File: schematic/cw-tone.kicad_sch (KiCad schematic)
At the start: 21 parts, among them Q14 2N7000, Q15 2N7000, U16 NE5532

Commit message: Minor changes
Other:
- moved on the sheet: C134, C135, C136, C137, C138, C139, C140, C141, D19, D20, Q14, Q15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

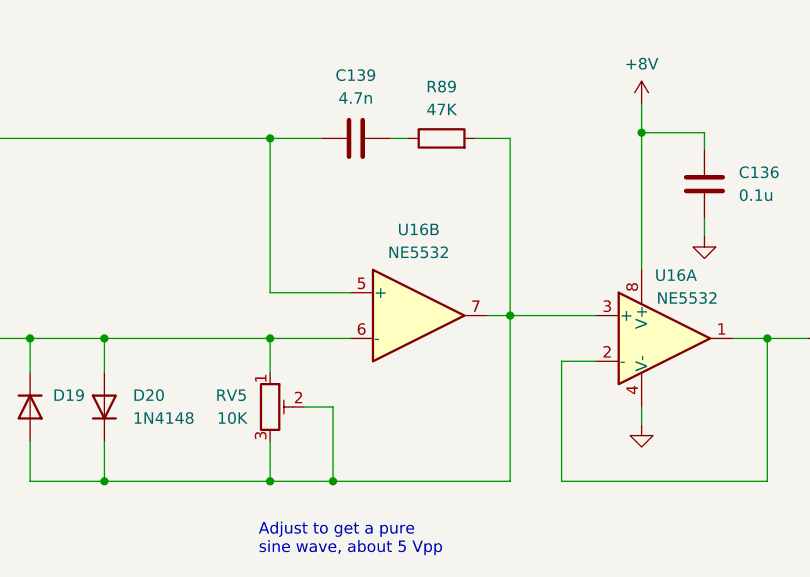
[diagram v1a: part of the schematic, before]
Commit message: Make CW tone frequency adjustable
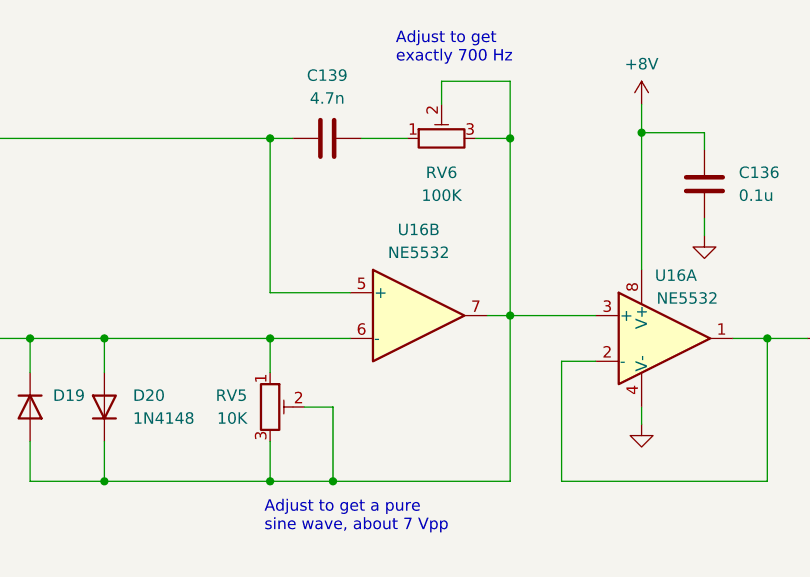
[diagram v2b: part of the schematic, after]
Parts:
- removed R89: 47K, symbol Device:R
- added RV6: 100K, symbol Device:R_Potentiometer_Trim
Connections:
- net at D19.2 (A), D20.1 (K), RV5.2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: now also RV6.2, RV6.3
- net at C139.2: now also RV6.1
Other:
- note added: "Adjust to get a pure sine wave, about 7 Vpp"
- note added: "Adjust to get exactly 700 Hz"
- note removed: "Adjust to get a pure sine wave, about 5 Vpp"
- moved on the sheet: C139
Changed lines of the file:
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@@
   (junction (at 77.47 99.695) (diameter 0) (color 0 0 0 0)
   )
+  (junction (at 130.81 77.47) (diameter 0) (color 0 0 0 0)
+  )
   (junction (at 130.81 97.155) (diameter 0) (color 0 0 0 0)
   )
+  (junction (at 85.725 99.695) (diameter 0) (color 0 0 0 0)
+  )
   (junction (at 104.14 77.47) (diameter 0) (color 0 0 0 0)
   )
-  (junction (at 85.725 99.695) (diameter 0) (color 0 0 0 0)
-  )
   (junction (at 210.185 71.12) (diameter 0) (color 0 0 0 0)
   )
@@
     (stroke (width 0) (type default))
   )
+  (wire (pts (xy 130.81 71.12) (xy 123.19 71.12))
+    (stroke (width 0) (type default))
+  )
   (wire (pts (xy 85.725 99.695) (xy 85.725 103.505))
     (stroke (width 0) (type default))
@@
     (stroke (width 0) (type default))
   )
+  (wire (pts (xy 127 77.47) (xy 130.81 77.47))
+    (stroke (width 0) (type default))
+  )
   (wire (pts (xy 111.125 115.57) (xy 111.125 107.315))
     (stroke (width 0) (type default))
@@
     (stroke (width 0) (type default))
   )
-  (wire (pts (xy 117.475 77.47) (xy 119.38 77.47))
+  (wire (pts (xy 104.14 77.47) (xy 106.68 77.47))
     (stroke (width 0) (type default))
   )
@@
     (stroke (width 0) (type default))
   )
-  (wire (pts (xy 130.81 77.47) (xy 127 77.47))
-    (stroke (width 0) (type default))
-  )
   (wire (pts (xy 62.23 99.695) (xy 66.04 99.695))
     (stroke (width 0) (type default))
@@
     (stroke (width 0) (type default))
   )
+  (wire (pts (xy 123.19 71.12) (xy 123.19 73.66))
+    (stroke (width 0) (type default))
+  )
   (wire (pts (xy 104.14 94.615) (xy 113.03 94.615))
     (stroke (width 0) (type default))
@@
     (stroke (width 0) (type default))
   )
+  (wire (pts (xy 114.3 77.47) (xy 119.38 77.47))
+    (stroke (width 0) (type default))
+  )
+  (wire (pts (xy 130.81 77.47) (xy 130.81 71.12))
+    (stroke (width 0) (type default))
+  )
   (wire (pts (xy 73.66 99.695) (xy 77.47 99.695))
     (stroke (width 0) (type default))
@@
   )
   (wire (pts (xy 62.23 104.14) (xy 62.23 99.695))
-    (stroke (width 0) (type default))
-  )
-  (wire (pts (xy 109.855 77.47) (xy 104.14 77.47))
     (stroke (width 0) (type default))
   )
@@
     (effects (font (size 1.27 1.27)) (justify left bottom))
   )
-  (text "Adjust to get a pure \nsine wave, about 5 Vpp" (at 102.87 123.825 0)
+  (text "Adjust to get a pure \nsine wave, about 7 Vpp" (at 103.505 121.285 0)
+    (effects (font (size 1.27 1.27)) (justify left bottom))
+  )
+  (text "Adjust to get\nexactly 700 Hz" (at 118.11 69.215 0)
     (effects (font (size 1.27 1.27)) (justify left bottom))
   )
@@
     )
   )
-  (symbol (lib_id "Device:R") (at 123.19 77.47 90) (unit 1)
-    (in_bom yes) (on_board yes) (dnp no) (fields_autoplaced)
-    (property "Reference" "R89" (at 123.19 71.755 90)
-      (effects (font (size 1.27 1.27)))
-    )
-    (property "Value" "47K" (at 123.19 74.295 90)
-      (effects (font (size 1.27 1.27)))
-    )
-    (property "Footprint" "" (at 123.19 79.248 90)
-      (effects (font (size 1.27 1.27)) hide)
-    )
-    (property "Datasheet" "~" (at 123.19 77.47 0)
-      (effects (font (size 1.27 1.27)) hide)
-    )
-    (pin "1")
-    (pin "2")
-    (instances
-      (project "hbr-mk2"
-        (path "/700c9878-4ed7-49d5-a273-77cf9d92989d/53c64ec8-e682-4447-a686-92e02593189c"
-          (reference "R89") (unit 1)
-        )
-      )
-    )
-  )
   (symbol (lib_id "power:GND") (at 50.165 114.3 0) (unit 1)
     (in_bom yes) (on_board yes) (dnp no) (fields_autoplaced)
@@
     )
   )
+  (symbol (lib_id "Device:R_Potentiometer_Trim") (at 123.19 77.47 90) (unit 1)
+    (in_bom yes) (on_board yes) (dnp no) (fields_autoplaced)
+    (property "Reference" "RV6" (at 123.19 81.28 90)
+      (effects (font (size 1.27 1.27)))
+    )
+    (property "Value" "100K" (at 123.19 83.82 90)
+      (effects (font (size 1.27 1.27)))
+    )
+    (property "Footprint" "" (at 123.19 77.47 0)
+      (effects (font (size 1.27 1.27)) hide)
+    )
+    (property "Datasheet" "~" (at 123.19 77.47 0)
+      (effects (font (size 1.27 1.27)) hide)
+    )
+    (pin "1")
+    (pin "2")
+    (pin "3")
+    (instances
+      (project "hbr-mk2"
+        (path "/700c9878-4ed7-49d5-a273-77cf9d92989d/53c64ec8-e682-4447-a686-92e02593189c"
+          (reference "RV6") (unit 1)
+        )
+      )
+    )
+  )
   (symbol (lib_id "power:GND") (at 152.4 88.265 0) (unit 1)
     (in_bom yes) (on_board yes) (dnp no) (fields_autoplaced)
@@
     )
   )
-  (symbol (lib_id "Device:C") (at 113.665 77.47 90) (unit 1)
-    (in_bom yes) (on_board yes) (dnp no) (fields_autoplaced)
-    (property "Reference" "C139" (at 113.665 70.485 90)
-      (effects (font (size 1.27 1.27)))
-    )
-    (property "Value" "4.7n" (at 113.665 73.025 90)
-      (effects (font (size 1.27 1.27)))
-    )
-    (property "Footprint" "" (at 117.475 76.5048 0)
-      (effects (font (size 1.27 1.27)) hide)
-    )
-    (property "Datasheet" "~" (at 113.665 77.47 0)
-      (effects (font (size 1.27 1.27)) hide)
-    )
+  (symbol (lib_id "Device:C") (at 110.49 77.47 90) (unit 1)
+    (in_bom yes) (on_board yes) (dnp no) (fields_autoplaced)
+    (property "Reference" "C139" (at 110.49 70.485 90)
+      (effects (font (size 1.27 1.27)))
+    )
+    (property "Value" "4.7n" (at 110.49 73.025 90)
+      (effects (font (size 1.27 1.27)))
+    )
+    (property "Footprint" "" (at 114.3 76.5048 0)
+      (effects (font (size 1.27 1.27)) hide)
+    )
+    (property "Datasheet" "~" (at 110.49 77.47 0)
+      (effects (font (size 1.27 1.27)) hide)
+    )

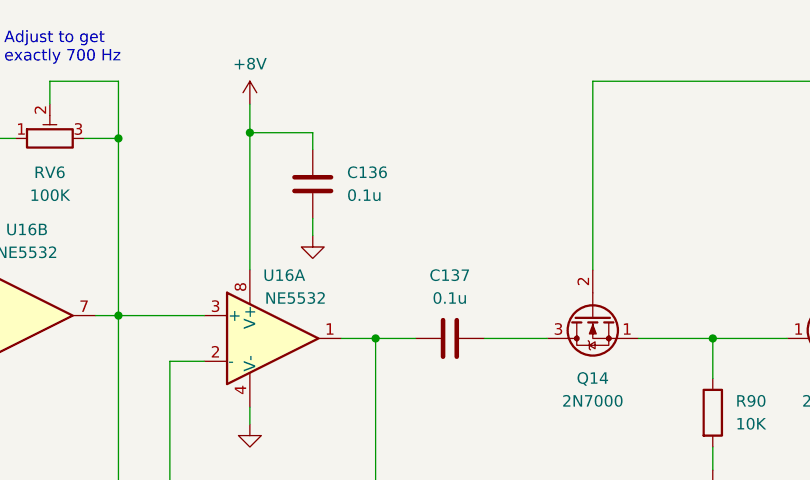
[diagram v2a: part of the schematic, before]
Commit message: Schematic: minor changes
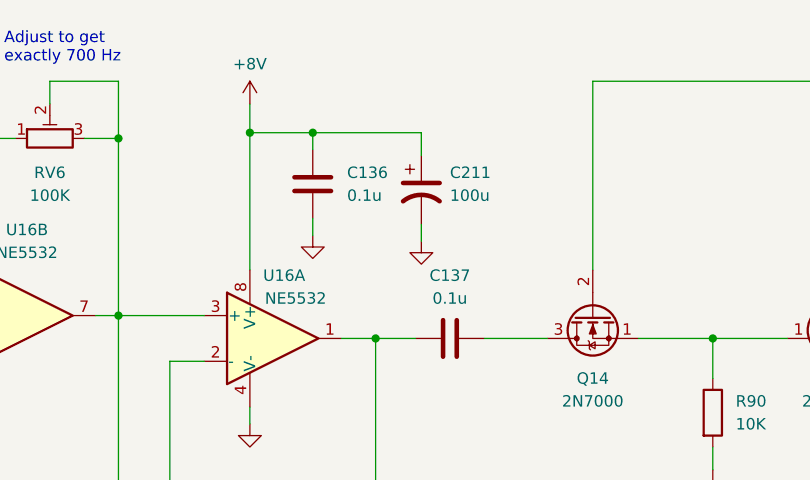
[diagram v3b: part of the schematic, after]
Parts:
- added C211: 100u, symbol Device:C_Polarized_US
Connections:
- net +8V: now also C211.1
- net GND: now also C211.2
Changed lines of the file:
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@@
   (junction (at 62.23 77.47) (diameter 0) (color 0 0 0 0)
   )
+  (junction (at 152.4 76.835) (diameter 0) (color 0 0 0 0)
+  )
   (junction (at 159.385 99.695) (diameter 0) (color 0 0 0 0)
   )
@@
     (stroke (width 0) (type default))
   )
+  (wire (pts (xy 164.465 86.995) (xy 164.465 88.9))
+    (stroke (width 0) (type default))
+  )
   (wire (pts (xy 85.725 115.57) (xy 104.14 115.57))
     (stroke (width 0) (type default))
@@
     (stroke (width 0) (type default))
   )
+  (wire (pts (xy 164.465 79.375) (xy 164.465 76.835))
+    (stroke (width 0) (type default))
+  )
   (wire (pts (xy 50.165 77.47) (xy 62.23 77.47))
     (stroke (width 0) (type default))
@@
   )
   (wire (pts (xy 130.81 77.47) (xy 130.81 71.12))
+    (stroke (width 0) (type default))
+  )
+  (wire (pts (xy 164.465 76.835) (xy 152.4 76.835))
     (stroke (width 0) (type default))
   )
@@
     )
   )
+  (symbol (lib_id "power:GND") (at 164.465 88.9 0) (unit 1)
+    (in_bom yes) (on_board yes) (dnp no) (fields_autoplaced)
+    (property "Reference" "#PWR0288" (at 164.465 95.25 0)
+      (effects (font (size 1.27 1.27)) hide)
+    )
+    (property "Value" "GND" (at 164.465 93.98 0)
+      (effects (font (size 1.27 1.27)) hide)
+    )
+    (property "Footprint" "" (at 164.465 88.9 0)
+      (effects (font (size 1.27 1.27)) hide)
+    )
+    (property "Datasheet" "" (at 164.465 88.9 0)
+      (effects (font (size 1.27 1.27)) hide)
+    )
+    (pin "1")
+    (instances
+      (project "hbr-mk2"
+        (path "/700c9878-4ed7-49d5-a273-77cf9d92989d/53c64ec8-e682-4447-a686-92e02593189c"
+          (reference "#PWR0288") (unit 1)
+        )
+      )
+    )
+  )
   (symbol (lib_id "Amplifier_Operational:NE5532") (at 120.65 97.155 0) (unit 2)
     (in_bom yes) (on_board yes) (dnp no) (fields_autoplaced)
@@
         )
       )
+    )
+  )
+  (symbol (lib_id "Device:C_Polarized_US") (at 164.465 83.185 0) (unit 1)
+    (in_bom yes) (on_board yes) (dnp no) (fields_autoplaced)
+    (property "Reference" "C211" (at 167.64 81.28 0)
+      (effects (font (size 1.27 1.27)) (justify left))
+    )
+    (property "Value" "100u" (at 167.64 83.82 0)
+      (effects (font (size 1.27 1.27)) (justify left))
+    )
+    (property "Footprint" "" (at 164.465 83.185 0)
+      (effects (font (size 1.27 1.27)) hide)
+    )
+    (property "Datasheet" "~" (at 164.465 83.185 0)
+      (effects (font (size 1.27 1.27)) hide)
+    )
+    (pin "1")
+    (pin "2")
+    (instances
+      (project "hbr-mk2"
+        (path "/700c9878-4ed7-49d5-a273-77cf9d92989d/53c64ec8-e682-4447-a686-92e02593189c"
+          (reference "C211") (unit 1)
+        )
+      )
